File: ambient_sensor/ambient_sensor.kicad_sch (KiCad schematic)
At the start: 24 parts, among them J1 Conn_01x02_Pin, J3 Conn_01x05_Pin, J4 Conn_01x01_Pin, J5 Conn_01x04_Pin, J6 Conn_01x02_Pin, U4 ATmega328-P, U6 LD1117S33TR_SOT223, Y1 Crystal

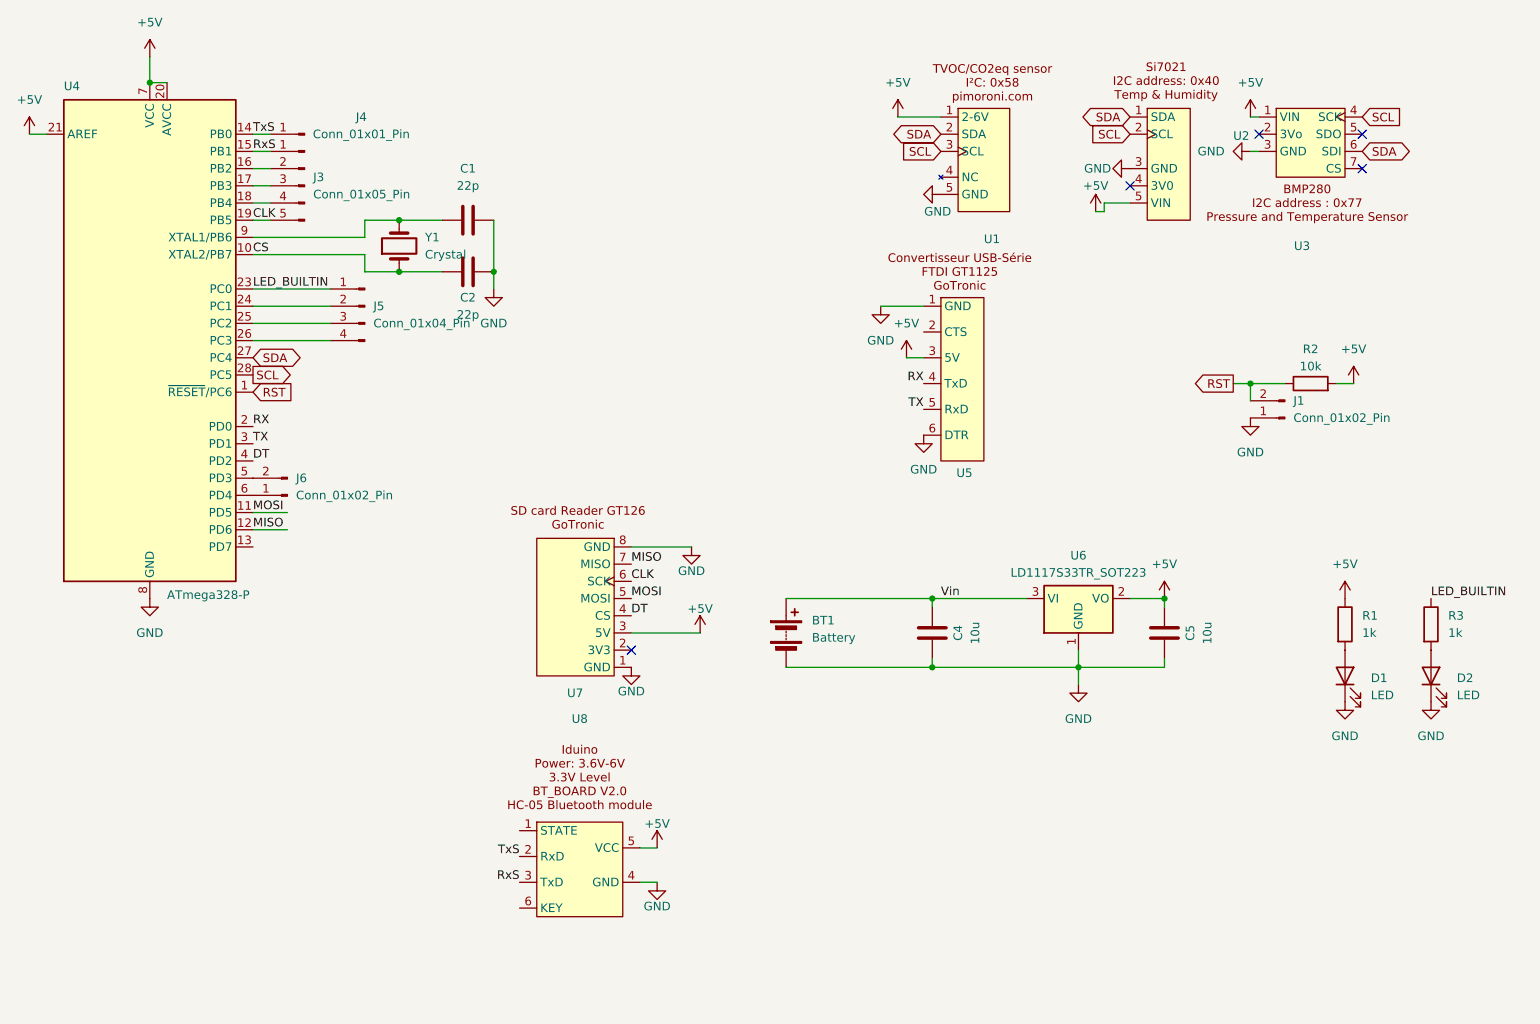
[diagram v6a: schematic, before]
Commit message: fixing the SD card reader
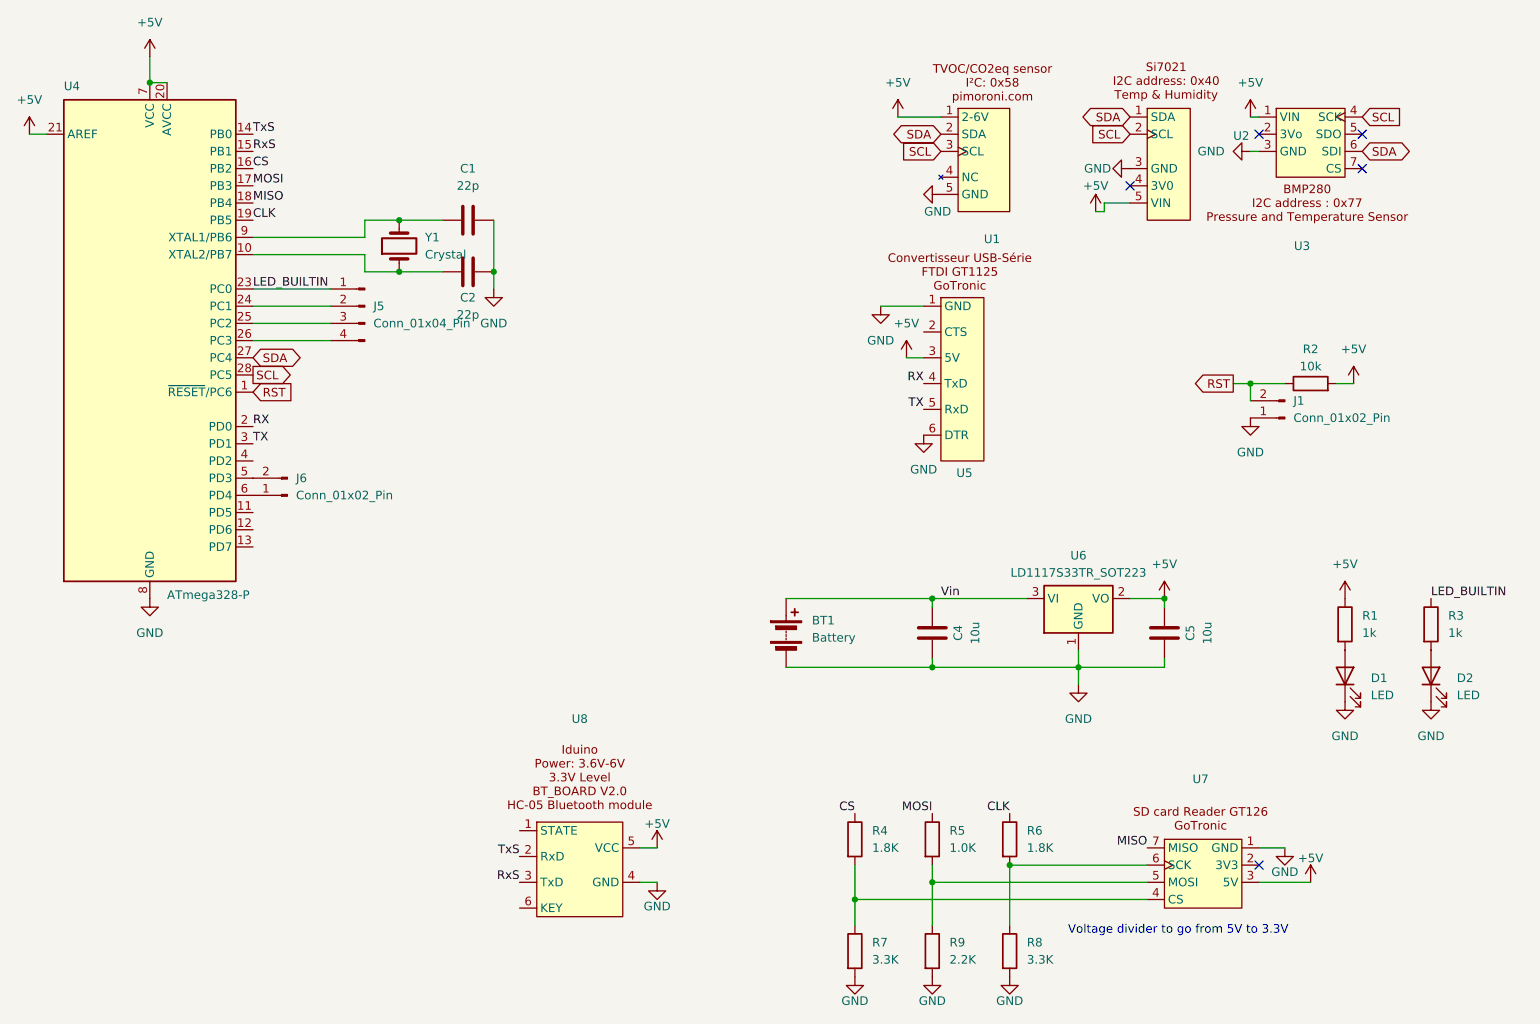
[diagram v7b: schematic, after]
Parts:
- removed J3: Conn_01x05_Pin, Connector_PinHeader_2.54mm:PinHeader_1x05_P2.54mm_Vertical, symbol Connector:Conn_01x05_Pin
- removed J4: Conn_01x01_Pin, Connector_PinHeader_2.54mm:PinHeader_1x01_P2.54mm_Vertical, symbol Connector:Conn_01x01_Pin
- added R4, R6: 1.8K, Resistor_SMD:R_1206_3216Metric, symbol Device:R
- added R5: 1.0K, Resistor_SMD:R_1206_3216Metric, symbol Device:R
- added R7, R8: 3.3K, Resistor_SMD:R_1206_3216Metric, symbol Device:R
- added R9: 2.2K, Resistor_SMD:R_1206_3216Metric, symbol Device:R
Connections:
- net CLK: now also R6.1; no longer U7.6 (SCK)
- net CS: now also U4.16 (PB2), R4.1; no longer C2.1, U4.10 (XTAL2/PB7), Y1.1
- net GND: now also R7.2, R8.2, R9.2; no longer U7.8 (GND)
- net MISO: now also U4.18 (PB4); no longer U4.12 (PD6)
- net MOSI: now also U4.17 (PB3), R5.1; no longer U4.11 (PD5), U7.5 (MOSI)
- net DT: no longer names the net of U7.4 (CS)
- net DT: now also R4.2, R7.1; no longer U4.4 (PD2)
- new net: C2.1, U4.10 (XTAL2/PB7), Y1.1
- new net: R5.2, R9.1, U7.5 (MOSI)
- new net: R6.2, R8.1, U7.6 (SCK)
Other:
- note added: "Voltage divider to go from 5V to 3.3V"

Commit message: fixing schematics
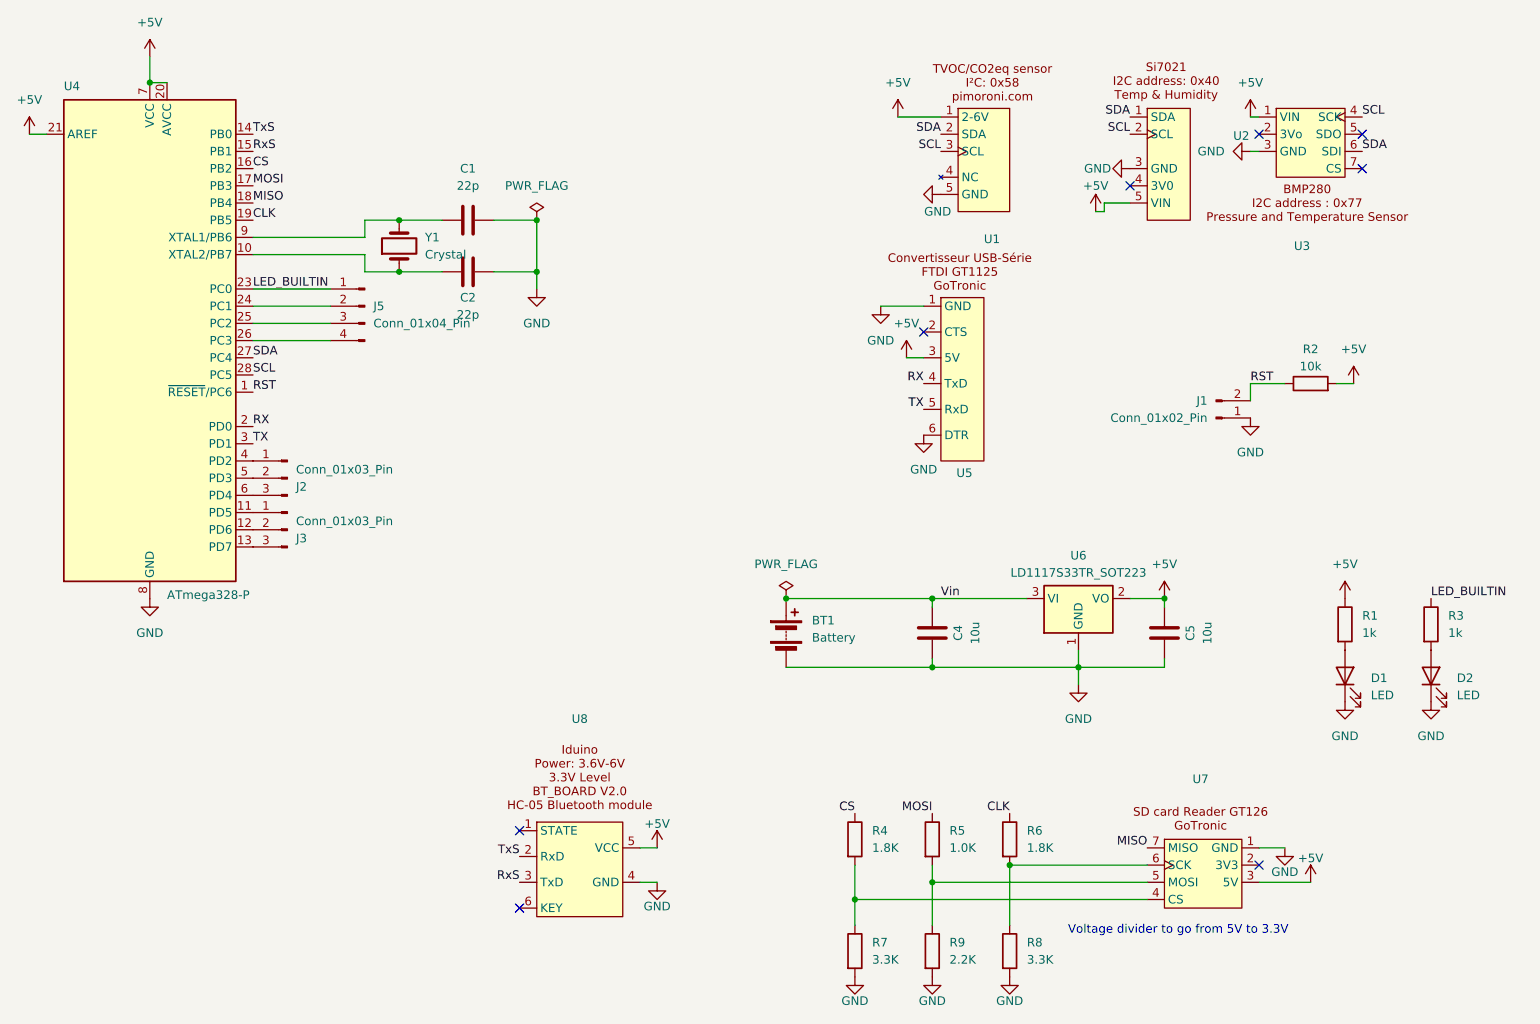
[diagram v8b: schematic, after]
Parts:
- removed J6: Conn_01x02_Pin, Connector_PinHeader_2.54mm:PinHeader_1x02_P2.54mm_Vertical, symbol Connector:Conn_01x02_Pin
- added J2, J3: Conn_01x03_Pin, Connector_PinHeader_2.54mm:PinHeader_1x03_P2.54mm_Vertical, symbol Connector:Conn_01x03_Pin
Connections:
- net at U4.6 (PD4): now also J2.3 (Pin_3)
- net at U4.5 (PD3): now also J2.2 (Pin_2)
- net at U4.11 (PD5): now also J3.1 (Pin_1)
- net at U4.12 (PD6): now also J3.2 (Pin_2)
- net at U4.13 (PD7): now also J3.3 (Pin_3)
- net at U4.4 (PD2): now also J2.1 (Pin_1)
- no-connect marks 5 -> 8
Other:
- moved on the sheet: J1
